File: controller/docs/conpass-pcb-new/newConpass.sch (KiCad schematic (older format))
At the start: 81 parts

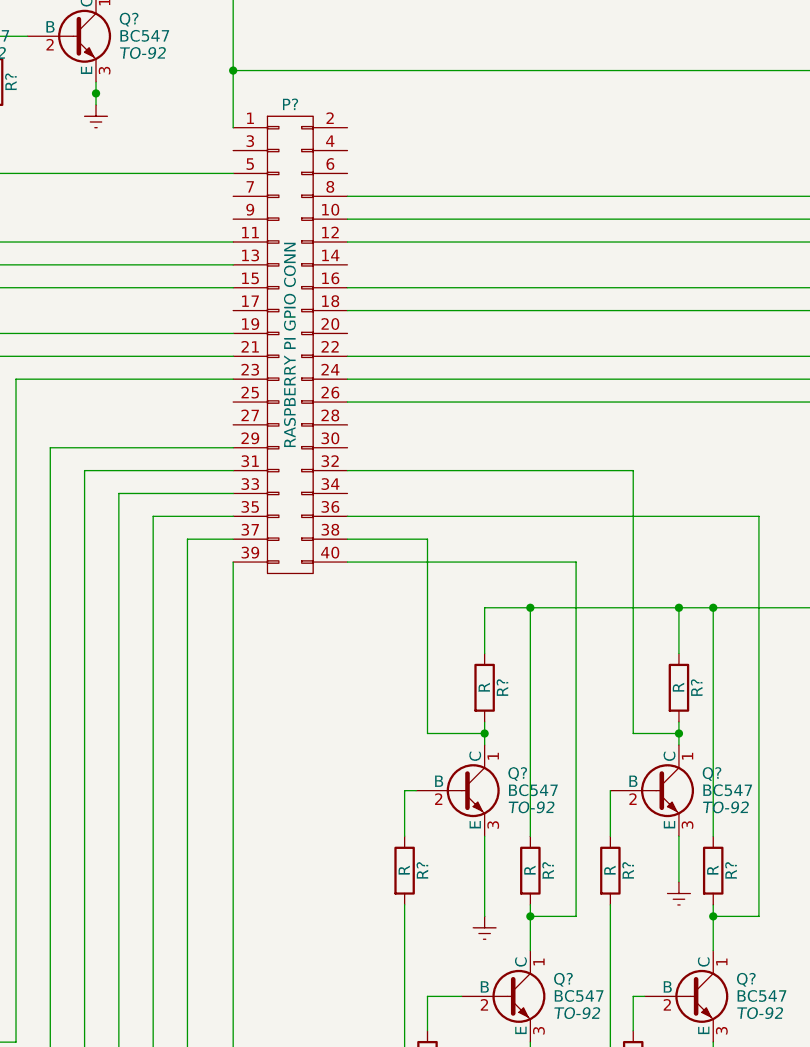
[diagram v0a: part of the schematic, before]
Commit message: Improve circuit schematic and fix some errors
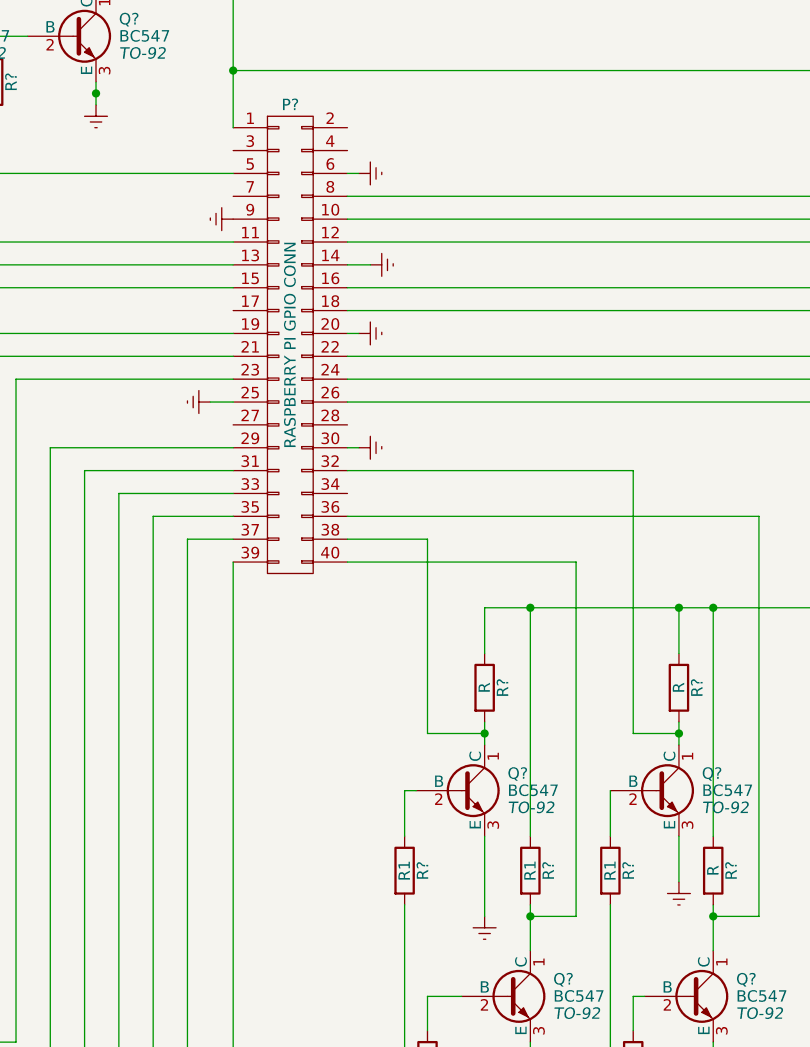
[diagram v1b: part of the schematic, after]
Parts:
- R? (x3): value R -> R1
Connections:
- net Earth: now also P?.14 (P14), P?.20 (P20), P?.25 (P25), P?.30 (P30), P?.6 (P6), P?.9 (P9)
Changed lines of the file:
@@
 P 7950 6300
 F 0 "R?" V 8030 6300 50  0000 C CNN
-F 1 "R" V 7950 6300 50  0000 C CNN
+F 1 "R1" V 7950 6300 50  0000 C CNN
 F 2 "" V 7880 6300 50  0000 C CNN
 F 3 "" H 7950 6300 50  0000 C CNN
@@
 P 8850 6300
 F 0 "R?" V 8930 6300 50  0000 C CNN
-F 1 "R" V 8850 6300 50  0000 C CNN
+F 1 "R1" V 8850 6300 50  0000 C CNN
 F 2 "" V 8780 6300 50  0000 C CNN
 F 3 "" H 8850 6300 50  0000 C CNN
@@
 P 8500 6300
 F 0 "R?" V 8580 6300 50  0000 C CNN
-F 1 "R" V 8500 6300 50  0000 C CNN
+F 1 "R1" V 8500 6300 50  0000 C CNN
 F 2 "" V 8430 6300 50  0000 C CNN
 F 3 "" H 8500 6300 50  0000 C CNN
@@
 	3750 8850 3750 7800
 Connection ~ 3150 8850
+$Comp
+L Earth #PWR?
+U 1 1 579636BE
+P 7750 4450
+F 0 "#PWR?" H 7750 4200 50  0001 C CNN
+F 1 "Earth" H 7750 4300 50  0001 C CNN
+F 2 "" H 7750 4450 50  0000 C CNN
+F 3 "" H 7750 4450 50  0000 C CNN
+	1    7750 4450
+	0    -1   -1   0
+$EndComp
+$Comp
+L Earth #PWR?
+U 1 1 57963774
+P 7750 3950
+F 0 "#PWR?" H 7750 3700 50  0001 C CNN
+F 1 "Earth" H 7750 3800 50  0001 C CNN
+F 2 "" H 7750 3950 50  0000 C CNN
+F 3 "" H 7750 3950 50  0000 C CNN
+	1    7750 3950
+	0    -1   -1   0
+$EndComp
+$Comp
+L Earth #PWR?
+U 1 1 5796382A
+P 7800 3650
+F 0 "#PWR?" H 7800 3400 50  0001 C CNN
+F 1 "Earth" H 7800 3500 50  0001 C CNN
+F 2 "" H 7800 3650 50  0000 C CNN
+F 3 "" H 7800 3650 50  0000 C CNN
+	1    7800 3650
+	0    -1   -1   0
+$EndComp
+$Comp
+L Earth #PWR?
+U 1 1 579638E0
+P 7750 3250
+F 0 "#PWR?" H 7750 3000 50  0001 C CNN
+F 1 "Earth" H 7750 3100 50  0001 C CNN
+F 2 "" H 7750 3250 50  0000 C CNN
+F 3 "" H 7750 3250 50  0000 C CNN
+	1    7750 3250
+	0    -1   -1   0
+$EndComp
+Wire Wire Line
+	7750 3250 7700 3250
+Wire Wire Line
+	7700 3650 7800 3650
+Wire Wire Line
+	7700 3950 7750 3950
+Wire Wire Line
+	7700 4450 7750 4450
+$Comp
+L Earth #PWR?
+U 1 1 57963FFF
+P 7100 4250
+F 0 "#PWR?" H 7100 4000 50  0001 C CNN
+F 1 "Earth" H 7100 4100 50  0001 C CNN
+F 2 "" H 7100 4250 50  0000 C CNN
+F 3 "" H 7100 4250 50  0000 C CNN
+	1    7100 4250
+	0    1    1    0
+$EndComp
+$Comp
+L Earth #PWR?
+U 1 1 579640B5
+P 7200 3450
+F 0 "#PWR?" H 7200 3200 50  0001 C CNN
+F 1 "Earth" H 7200 3300 50  0001 C CNN
+F 2 "" H 7200 3450 50  0000 C CNN
+F 3 "" H 7200 3450 50  0000 C CNN
+	1    7200 3450
+	0    1    1    0
+$EndComp
+Wire Wire Line
+	7100 4250 7200 4250
 $EndSCHEMATC
